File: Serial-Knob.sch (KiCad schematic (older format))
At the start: 16 parts, among them IC1 ATtiny85, P1 CONN_4

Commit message: Blah.
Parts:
- added P2: ISP, symbol CONN_4
- R4: value 4k7 -> 1k
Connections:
- net MISO: now also P2.3 (P3)
- net MOSI: now also P2.4 (P4)
- net RESET: now also P2.1 (P1)
- net SCK: now also P2.2 (P2)
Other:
- moved on the sheet: MH1, MH2, MH3, MH4
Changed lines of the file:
@@
-EESchema Schematic File Version 2  date Tue 22 Jan 2013 11:04:26 AM CET
+EESchema Schematic File Version 2  date Tue 22 Jan 2013 11:50:57 AM CET
 LIBS:my_parts
 LIBS:power
@@
 P 6250 2750
 F 0 "R4" V 6330 2750 50  0000 C CNN
-F 1 "4k7" V 6250 2750 50  0000 C CNN
+F 1 "1k" V 6250 2750 50  0000 C CNN
 	1    6250 2750
 	-1   0    0    1
@@
 L CONN_1 MH1
 U 1 1 50FE4BC1
-P 4600 3850
-F 0 "MH1" H 4680 3850 40  0000 L CNN
-F 1 "CONN_1" H 4600 3905 30  0001 C CNN
-	1    4600 3850
+P 6700 850
+F 0 "MH1" H 6780 850 40  0000 L CNN
+F 1 "CONN_1" H 6700 905 30  0001 C CNN
+	1    6700 850
 	1    0    0    -1
 $EndComp
@@
 L CONN_1 MH2
 U 1 1 50FE4BD0
-P 4600 3950
-F 0 "MH2" H 4680 3950 40  0000 L CNN
-F 1 "CONN_1" H 4600 4005 30  0001 C CNN
-	1    4600 3950
+P 6700 950
+F 0 "MH2" H 6780 950 40  0000 L CNN
+F 1 "CONN_1" H 6700 1005 30  0001 C CNN
+	1    6700 950
 	1    0    0    -1
 $EndComp
@@
 L CONN_1 MH3
 U 1 1 50FE4BDF
-P 4600 4050
-F 0 "MH3" H 4680 4050 40  0000 L CNN
-F 1 "CONN_1" H 4600 4105 30  0001 C CNN
-	1    4600 4050
+P 6700 1050
+F 0 "MH3" H 6780 1050 40  0000 L CNN
+F 1 "CONN_1" H 6700 1105 30  0001 C CNN
+	1    6700 1050
 	1    0    0    -1
 $EndComp
@@
 L CONN_1 MH4
 U 1 1 50FE4BEE
-P 4600 4150
-F 0 "MH4" H 4680 4150 40  0000 L CNN
-F 1 "CONN_1" H 4600 4205 30  0001 C CNN
-	1    4600 4150
-	1    0    0    -1
-$EndComp
-NoConn ~ 4450 4150
-NoConn ~ 4450 4050
-NoConn ~ 4450 3950
-NoConn ~ 4450 3850
+P 6700 1150
+F 0 "MH4" H 6780 1150 40  0000 L CNN
+F 1 "CONN_1" H 6700 1205 30  0001 C CNN
+	1    6700 1150
+	1    0    0    -1
+$EndComp
+NoConn ~ 6550 1150
+NoConn ~ 6550 1050
+NoConn ~ 6550 950
+NoConn ~ 6550 850
 $Comp
 L R R5
@@
 Wire Wire Line
 	1800 1500 1900 1500
+Text Label 4300 3650 0    60   ~ 0
+MOSI
+Text Label 4300 3750 0    60   ~ 0
+MISO
+Text Label 4300 3850 0    60   ~ 0
+SCK
+Text Label 4300 3950 0    60   ~ 0
+RESET
+$Comp
+L CONN_4 P2
+U 1 1 50FE6A12
+P 3950 3800
+F 0 "P2" V 3900 3800 50  0000 C CNN
+F 1 "ISP" V 4000 3800 50  0000 C CNN
+	1    3950 3800
+	-1   0    0    1
+$EndComp
 $EndSCHEMATC

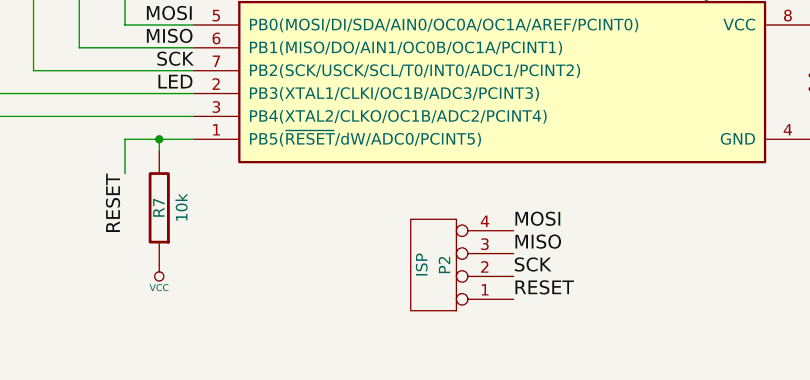
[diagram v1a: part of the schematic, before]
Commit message: Added a 6-pin ISP header - 2mm raster ;-(
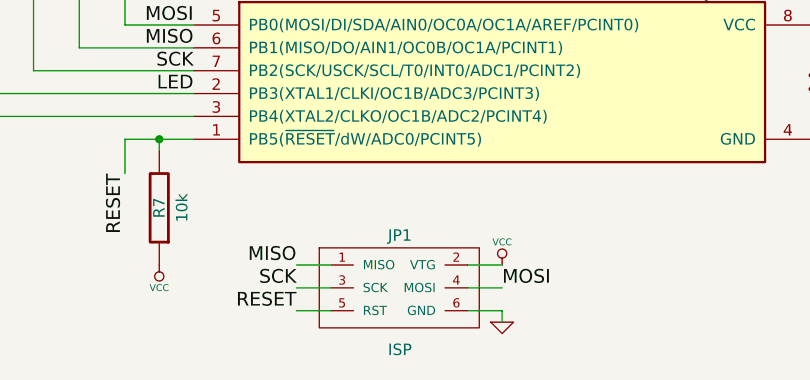
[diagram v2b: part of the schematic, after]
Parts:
- removed P2: ISP, symbol CONN_4
- added JP1: ISP, symbol MADW__AVR_ISP
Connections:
- net GND: now also JP1.6 (GND)
- net MISO: now also JP1.1 (MISO)
- net MOSI: now also JP1.4 (MOSI)
- net RESET: now also JP1.5 (RST)
- net SCK: now also JP1.3 (SCK)
- net VCC: now also JP1.2 (VTG)
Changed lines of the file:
@@
-EESchema Schematic File Version 2  date Tue 22 Jan 2013 11:50:57 AM CET
+EESchema Schematic File Version 2  date Tue 22 Jan 2013 11:47:59 PM CET
 LIBS:my_parts
 LIBS:power
@@
 Wire Wire Line
 	1800 1500 1900 1500
-Text Label 4300 3650 0    60   ~ 0
+Text Label 4250 3900 0    60   ~ 0
 MOSI
-Text Label 4300 3750 0    60   ~ 0
+Text Label 3350 3800 2    60   ~ 0
 MISO
-Text Label 4300 3850 0    60   ~ 0
+Text Label 3350 3900 2    60   ~ 0
 SCK
-Text Label 4300 3950 0    60   ~ 0
+Text Label 3350 4000 2    60   ~ 0
 RESET
 $Comp
-L CONN_4 P2
-U 1 1 50FE6A12
-P 3950 3800
-F 0 "P2" V 3900 3800 50  0000 C CNN
-F 1 "ISP" V 4000 3800 50  0000 C CNN
-	1    3950 3800
-	-1   0    0    1
-$EndComp
+L MADW__AVR_ISP JP1
+U 1 1 50FF0EC2
+P 3800 3900
+F 0 "JP1" H 3750 4100 50  0000 L BNN
+F 1 "ISP" H 3750 3600 50  0000 L BNN
+	1    3800 3900
+	1    0    0    -1
+$EndComp
+$Comp
+L VCC #PWR013
+U 1 1 50FF0F17
+P 4250 3800
+F 0 "#PWR013" H 4250 3900 30  0001 C CNN
+F 1 "VCC" H 4250 3900 30  0000 C CNN
+	1    4250 3800
+	1    0    0    -1
+$EndComp
+$Comp
+L GND #PWR014
+U 1 1 50FF0F26
+P 4250 4050
+F 0 "#PWR014" H 4250 4050 30  0001 C CNN
+F 1 "GND" H 4250 3980 30  0001 C CNN
+	1    4250 4050
+	1    0    0    -1
+$EndComp
+Wire Wire Line
+	4100 3800 4250 3800
+Wire Wire Line
+	4100 3900 4250 3900
+Wire Wire Line
+	4100 4000 4250 4000
+Wire Wire Line
+	4250 4000 4250 4050
+Wire Wire Line
+	3350 4000 3500 4000
+Wire Wire Line
+	3500 3900 3350 3900
+Wire Wire Line
+	3500 3800 3350 3800
 $EndSCHEMATC

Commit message: Switched to REV. 202 of atmel.lib
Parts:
- removed IC1: ATtiny85, DIP8, symbol ATTINY85-P
- added IC1: ATTINY85-S, SO8-200, symbol ATTINY85-S
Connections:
- net GND: now also IC1.4 (GND)
- net LED: now also IC1.2 (PB3(XTAL1/CLKI/OC1B/ADC3/PCINT3))
- net MISO: now also IC1.6 (PB1(MISO/DO/AIN1/OC0B/OC1A/PCINT1))
- net MOSI: now also IC1.5 (PB0(MOSI/DI/SDA/AIN0/OC0A/OC1A/AREF/PCINT0))
- net RESET: now also IC1.1 (PB5(~RESET~/dW/ADC0/PCINT5))
- net SCK: now also IC1.7 (PB2(SCK/USCK/SCL/T0/INT0/ADC1/PCINT2))
- net VCC: now also IC1.8 (VCC)
- net at R6.2: now also IC1.3 (PB4(XTAL2/CLKO/OC1B/ADC2/PCINT4))
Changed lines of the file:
@@
-EESchema Schematic File Version 2  date Tue 22 Jan 2013 11:47:59 PM CET
+EESchema Schematic File Version 2  date Sun 27 Jan 2013 10:13:45 AM CET
 LIBS:my_parts
 LIBS:power
@@
 LIBS:contrib
 LIBS:valves
-LIBS:atmel_rev110
-LIBS:murata-resonators
 LIBS:Serial-Knob-cache
 EELAYER 27 0
@@
 Sheet 1 1
 Title "Serial Knob"
-Date "22 jan 2013"
+Date "27 jan 2013"
 Rev "0.1"
 Comp "2013 - blog.spitzenpfeil.org"
@@
 	1    2750 3550
 	-1   0    0    1
-$EndComp
-$Comp
-L ATTINY85-P IC1
-U 1 1 4F6EC673
-P 3100 2650
-F 0 "IC1" H 3200 2700 60  0000 C CNN
-F 1 "ATtiny85" H 5100 2700 60  0000 C CNN
-F 2 "DIP8" H 3200 1900 60  0001 C CNN
-	1    3100 2650
-	1    0    0    -1
 $EndComp
 Connection ~ 2750 3250
@@
 Wire Wire Line
 	3500 3800 3350 3800
+$Comp
+L ATTINY85-S IC1
+U 1 1 5104EF69
+P 4250 3000
+F 0 "IC1" H 3200 3400 60  0000 C CNN
+F 1 "ATTINY85-S" H 5100 2600 60  0000 C CNN
+F 2 "SO8-200" H 3350 2600 60  0000 C CNN
+	1    4250 3000
+	1    0    0    -1
+$EndComp
 $EndSCHEMATC

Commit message: Some behind the scenes stuff. Layout unchanged.
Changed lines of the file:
@@
-EESchema Schematic File Version 2  date Sun 27 Jan 2013 10:13:45 AM CET
+EESchema Schematic File Version 2  date Sat 23 Feb 2013 05:53:57 PM CET
 LIBS:my_parts
 LIBS:power
@@
 Sheet 1 1
 Title "Serial Knob"
-Date "27 jan 2013"
+Date "23 feb 2013"
 Rev "0.1"
 Comp "2013 - blog.spitzenpfeil.org"
@@
 F 0 "C1" H 5750 3100 50  0000 L CNN
 F 1 "4µ7" H 5750 2900 50  0000 L CNN
+F 2 "" H 5700 3000 60  0001 C CNN
+F 3 "" H 5700 3000 60  0001 C CNN
 	1    5700 3000
 	1    0    0    -1
@@
 F 0 "#PWR01" H 5700 2850 30  0001 C CNN
 F 1 "VCC" H 5700 2850 30  0000 C CNN
+F 2 "" H 5700 2750 60  0001 C CNN
+F 3 "" H 5700 2750 60  0001 C CNN
 	1    5700 2750
 	1    0    0    -1
@@
 F 0 "#PWR02" H 5700 3300 30  0001 C CNN
 F 1 "GND" H 5700 3230 30  0001 C CNN
+F 2 "" H 5700 3300 60  0001 C CNN
+F 3 "" H 5700 3300 60  0001 C CNN
 	1    5700 3300
 	1    0    0    -1
@@
 F 0 "#PWR03" H 2750 3900 30  0001 C CNN
 F 1 "VCC" H 2750 3900 30  0000 C CNN
+F 2 "" H 2750 3800 60  0001 C CNN
+F 3 "" H 2750 3800 60  0001 C CNN
 	1    2750 3800
 	-1   0    0    1
@@
 F 0 "R7" V 2750 3550 50  0000 C CNN
 F 1 "10k" V 2650 3550 50  0000 C CNN
+F 2 "" H 2750 3550 60  0001 C CNN
+F 3 "" H 2750 3550 60  0001 C CNN
 	1    2750 3550
 	-1   0    0    1
@@
 F 0 "#FLG04" H 7100 1095 30  0001 C CNN
 F 1 "PWR_FLAG" H 7100 1200 30  0000 C CNN
+F 2 "" H 7100 1000 60  0001 C CNN
+F 3 "" H 7100 1000 60  0001 C CNN
 	1    7100 1000
 	1    0    0    -1
@@
 F 0 "#PWR05" H 7100 1150 30  0001 C CNN
 F 1 "GND" H 7100 1080 30  0001 C CNN
+F 2 "" H 7100 1150 60  0001 C CNN
+F 3 "" H 7100 1150 60  0001 C CNN
 	1    7100 1150
 	1    0    0    -1
@@
 F 0 "D1" H 6250 3350 50  0000 C CNN
 F 1 "LED" H 6250 3150 50  0000 C CNN
+F 2 "" H 6250 3250 60  0001 C CNN
+F 3 "" H 6250 3250 60  0001 C CNN
 	1    6250 3250
 	0    1    1    0
@@
 F 0 "#PWR06" H 6250 3500 30  0001 C CNN
 F 1 "GND" H 6250 3430 30  0001 C CNN
+F 2 "" H 6250 3500 60  0001 C CNN
+F 3 "" H 6250 3500 60  0001 C CNN
 	1    6250 3500
 	1    0    0    -1
@@
 F 0 "R4" V 6330 2750 50  0000 C CNN
 F 1 "1k" V 6250 2750 50  0000 C CNN
+F 2 "" H 6250 2750 60  0001 C CNN
+F 3 "" H 6250 2750 60  0001 C CNN
 	1    6250 2750
 	-1   0    0    1
@@
 Wire Wire Line
 	6250 3050 6250 3000
-$Comp
-L MADW__ALPS-STEC12E08 ENC1
-U 1 1 50FE4588
-P 4050 2050
-F 0 "ENC1" H 4050 2425 60  0000 C CNN
-F 1 "ALPS-STEC12E08" H 4050 2550 60  0000 C CNN
-	1    4050 2050
-	1    0    0    -1
-$EndComp
 Wire Wire Line
 	6250 2450 6250 2500
@@
 F 0 "#PWR07" H 3450 2300 30  0001 C CNN
 F 1 "GND" H 3450 2230 30  0001 C CNN
+F 2 "" H 3450 2300 60  0001 C CNN
+F 3 "" H 3450 2300 60  0001 C CNN
 	1    3450 2300
 	1    0    0    -1
@@
 F 0 "#PWR08" H 4700 2100 30  0001 C CNN
 F 1 "GND" H 4700 2030 30  0001 C CNN
+F 2 "" H 4700 2100 60  0001 C CNN
+F 3 "" H 4700 2100 60  0001 C CNN
 	1    4700 2100
 	1    0    0    -1
@@
 F 0 "R1" V 2280 2350 50  0000 C CNN
 F 1 "1k" V 2200 2350 50  0000 C CNN
+F 2 "" H 2200 2350 60  0001 C CNN
+F 3 "" H 2200 2350 60  0001 C CNN
 	1    2200 2350
 	1    0    0    -1
@@
 F 0 "R2" V 2480 2350 50  0000 C CNN
 F 1 "1k" V 2400 2350 50  0000 C CNN
+F 2 "" H 2400 2350 60  0001 C CNN
+F 3 "" H 2400 2350 60  0001 C CNN
 	1    2400 2350
 	1    0    0    -1
@@
 F 0 "R3" V 2680 2350 50  0000 C CNN
 F 1 "1k" V 2600 2350 50  0000 C CNN
+F 2 "" H 2600 2350 60  0001 C CNN
+F 3 "" H 2600 2350 60  0001 C CNN
 	1    2600 2350
 	1    0    0    -1
@@
 F 0 "P1" V 1600 1150 50  0000 C CNN
 F 1 "CONN_4" V 1700 1150 50  0000 C CNN
+F 2 "" H 1650 1150 60  0001 C CNN
+F 3 "" H 1650 1150 60  0001 C CNN
 	1    1650 1150
 	0    -1   -1   0
@@
 F 0 "#PWR09" H 1450 1600 30  0001 C CNN
 F 1 "GND" H 1450 1530 30  0001 C CNN
+F 2 "" H 1450 1600 60  0001 C CNN
+F 3 "" H 1450 1600 60  0001 C CNN
 	1    1450 1600
 	0    1    1    0
@@
 F 0 "#PWR010" H 1600 1700 30  0001 C CNN
 F 1 "VCC" H 1600 1700 30  0000 C CNN
+F 2 "" H 1600 1600 60  0001 C CNN
+F 3 "" H 1600 1600 60  0001 C CNN
 	1    1600 1600
 	-1   0    0    1
@@
 F 0 "MH1" H 6780 850 40  0000 L CNN
 F 1 "CONN_1" H 6700 905 30  0001 C CNN
+F 2 "" H 6700 850 60  0001 C CNN
+F 3 "" H 6700 850 60  0001 C CNN
 	1    6700 850
 	1    0    0    -1
@@
 F 0 "MH2" H 6780 950 40  0000 L CNN
 F 1 "CONN_1" H 6700 1005 30  0001 C CNN
+F 2 "" H 6700 950 60  0001 C CNN
+F 3 "" H 6700 950 60  0001 C CNN
 	1    6700 950
 	1    0    0    -1
@@
 F 0 "MH3" H 6780 1050 40  0000 L CNN
 F 1 "CONN_1" H 6700 1105 30  0001 C CNN
+F 2 "" H 6700 1050 60  0001 C CNN
+F 3 "" H 6700 1050 60  0001 C CNN
 	1    6700 1050
 	1    0    0    -1
@@
 F 0 "MH4" H 6780 1150 40  0000 L CNN
 F 1 "CONN_1" H 6700 1205 30  0001 C CNN
+F 2 "" H 6700 1150 60  0001 C CNN
+F 3 "" H 6700 1150 60  0001 C CNN
 	1    6700 1150
 	1    0    0    -1
@@
 F 0 "R5" V 1980 2350 50  0000 C CNN
 F 1 "1k" V 1900 2350 50  0000 C CNN
+F 2 "" H 1900 2350 60  0001 C CNN
+F 3 "" H 1900 2350 60  0001 C CNN
 	1    1900 2350
 	1    0    0    -1
@@
 F 0 "R6" V 1780 2350 50  0000 C CNN
 F 1 "1k" V 1700 2350 50  0000 C CNN
+F 2 "" H 1700 2350 60  0001 C CNN
+F 3 "" H 1700 2350 60  0001 C CNN
 	1    1700 2350
 	1    0    0    -1
@@
 F 0 "#FLG011" H 7350 1095 30  0001 C CNN
 F 1 "PWR_FLAG" H 7350 1180 30  0000 C CNN
+F 2 "" H 7350 1000 60  0001 C CNN
+F 3 "" H 7350 1000 60  0001 C CNN
 	1    7350 1000
 	1    0    0    -1
@@
 F 0 "#PWR012" H 7350 1250 30  0001 C CNN
 F 1 "VCC" H 7350 1250 30  0000 C CNN
+F 2 "" H 7350 1150 60  0001 C CNN
+F 3 "" H 7350 1150 60  0001 C CNN
 	1    7350 1150
 	-1   0    0    1
@@
 F 0 "JP1" H 3750 4100 50  0000 L BNN
 F 1 "ISP" H 3750 3600 50  0000 L BNN
+F 2 "" H 3800 3900 60  0001 C CNN
+F 3 "" H 3800 3900 60  0001 C CNN
 	1    3800 3900
 	1    0    0    -1
@@
 F 0 "#PWR013" H 4250 3900 30  0001 C CNN
 F 1 "VCC" H 4250 3900 30  0000 C CNN
+F 2 "" H 4250 3800 60  0001 C CNN
+F 3 "" H 4250 3800 60  0001 C CNN
 	1    4250 3800
 	1    0    0    -1
@@
 F 0 "#PWR014" H 4250 4050 30  0001 C CNN
 F 1 "GND" H 4250 3980 30  0001 C CNN
+F 2 "" H 4250 4050 60  0001 C CNN
+F 3 "" H 4250 4050 60  0001 C CNN
 	1    4250 4050
 	1    0    0    -1
@@
 F 1 "ATTINY85-S" H 5100 2600 60  0000 C CNN
 F 2 "SO8-200" H 3350 2600 60  0000 C CNN
+F 3 "" H 4250 3000 60  0001 C CNN
 	1    4250 3000
 	1    0    0    -1
 $EndComp
+$Comp
+L MADW__ALPS-STEC12E08 ENC1
+U 1 1 5128F4BC
+P 4050 2050
+F 0 "ENC1" H 4050 2425 60  0000 C CNN
+F 1 "ALPS-STEC12E08" H 4000 2550 60  0000 C CNN
+F 2 "" H 4050 2050 60  0000 C CNN
+F 3 "" H 4050 2050 60  0000 C CNN
+	1    4050 2050
+	1    0    0    -1
+$EndComp
